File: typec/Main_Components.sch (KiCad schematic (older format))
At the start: 13 parts

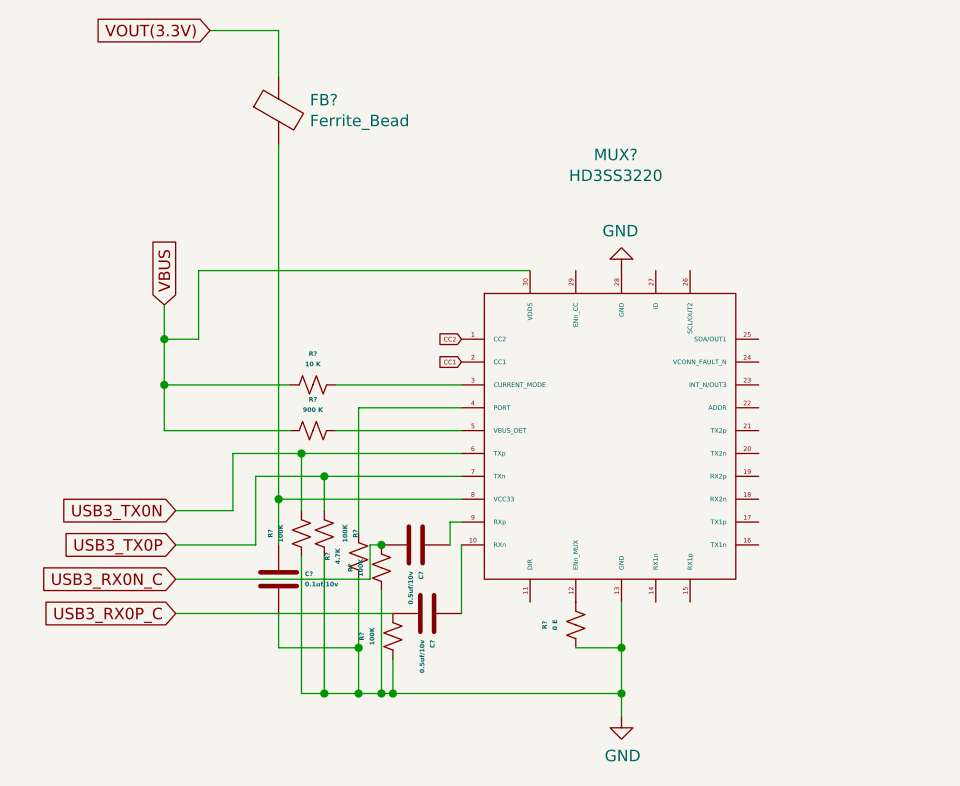
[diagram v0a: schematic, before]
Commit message: Added another page and completed the Multiplexer schematics.
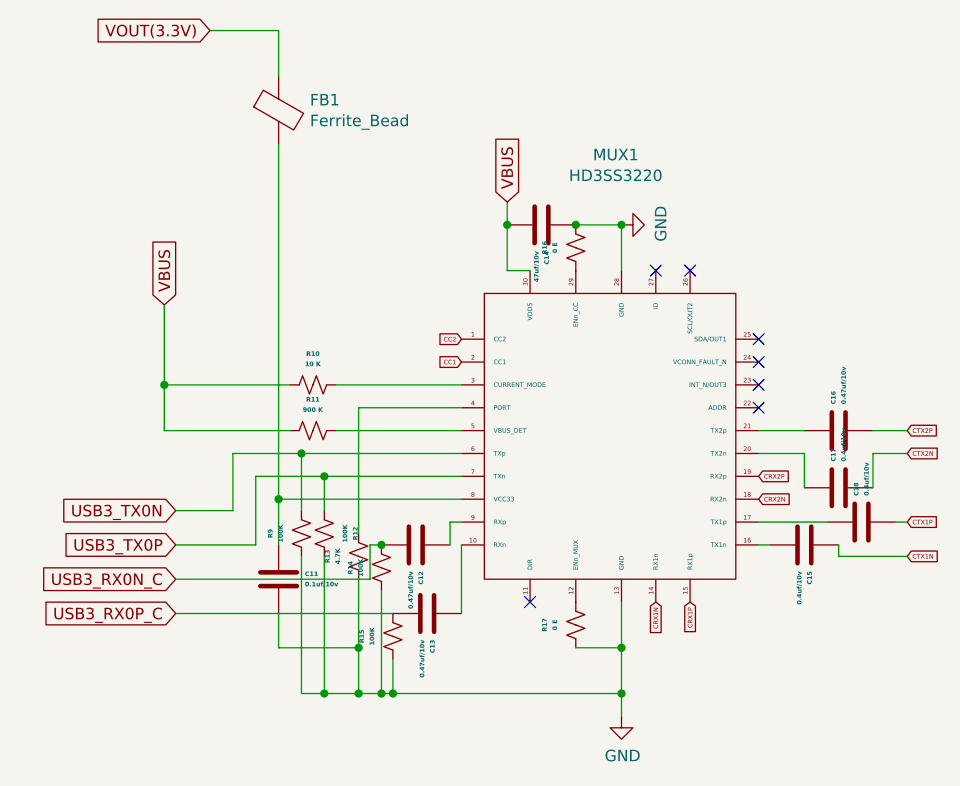
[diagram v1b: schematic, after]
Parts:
- added C14: 47uf/10v, Capacitor_SMD:C_0805_2012Metric, symbol Device:C
- added C15, C17, C18: 0.4uf/10v, Capacitor_SMD:C_0201_0603Metric, symbol Device:C
- added C16: 0.47uf/10v, Capacitor_SMD:C_0201_0603Metric, symbol Device:C
- added R16: 0 E, Resistor_SMD:R_0805_2012Metric, symbol Device:R_Small_US
- C12, C13: renamed from C?; value 0.5uf/10v -> 0.47uf/10v; footprint Capacitor_SMD:C_0805_2012Metric -> Capacitor_SMD:C_0201_0603Metric
- FB1: renamed from FB?; footprint (none) -> Inductor_SMD:L_0805_2012Metric
- MUX1: renamed from MUX?; footprint (none) -> HD3SS3220-VQFN:HD3SS3220-VQFN-MUX
- gave numbers to parts that had none: 9
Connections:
- net GND: now also C14.1, R16.1
- net VBUS: now also C14.2
- net CRX1N: now reaches MUX1.14 (RX1n)
- net CRX1P: now reaches MUX1.15 (RX1p)
- net at MUX1.16 (TX1n): now also C15.2
- net at MUX1.17 (TX1p): now also C18.1
- net CRX2N: now reaches MUX1.18 (RX2n)
- net CRX2P: now reaches MUX1.19 (RX2p)
- net at MUX1.20 (TX2n): now also C17.1
- net at MUX1.21 (TX2p): now also C16.1
- net at MUX1.29 (ENn_CC): now also R16.2
- new net CTX1N: C15.1
- new net CTX1P: C18.2
- new net CTX2N: C17.2
- new net CTX2P: C16.2
- no-connect marks 0 -> 7
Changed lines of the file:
@@
 $EndDescr
 $Comp
-L HD3SS3220-VQFN:HD3SS3220 MUX?
+L HD3SS3220-VQFN:HD3SS3220 MUX1
 U 1 1 5CC0E7BE
 P 4150 4200
-F 0 "MUX?" H 4175 5406 50  0000 C CNN
+F 0 "MUX1" H 4175 5406 50  0000 C CNN
 F 1 "HD3SS3220" H 4175 5315 50  0000 C CNN
-F 2 "" H 4800 3550 50  0001 C CNN
+F 2 "HD3SS3220-VQFN:HD3SS3220-VQFN-MUX" H 4800 3550 50  0001 C CNN
 F 3 "" H 4800 3550 50  0001 C CNN
 	1    4150 4200
@@
 P 4200 5450
 AR Path="/5CC20336" Ref="#PWR?"  Part="1"
-AR Path="/5CC0E3D3/5CC20336" Ref="#PWR?"  Part="1"
-F 0 "#PWR?" H 4200 5200 50  0001 C CNN
+AR Path="/5CC0E3D3/5CC20336" Ref="#PWR0108"  Part="1"
+F 0 "#PWR0108" H 4200 5200 50  0001 C CNN
 F 1 "GND" H 4205 5277 50  0000 C CNN
 F 2 "" H 4200 5450 50  0001 C CNN
@@
 L power:GND #PWR?
 U 1 1 5CC203FA
-P 4200 3500
+P 4200 3300
 AR Path="/5CC203FA" Ref="#PWR?"  Part="1"
-AR Path="/5CC0E3D3/5CC203FA" Ref="#PWR?"  Part="1"
-F 0 "#PWR?" H 4200 3250 50  0001 C CNN
-F 1 "GND" H 4205 3327 50  0000 C CNN
-F 2 "" H 4200 3500 50  0001 C CNN
-F 3 "" H 4200 3500 50  0001 C CNN
-	1    4200 3500
-	-1   0    0    1
+AR Path="/5CC0E3D3/5CC203FA" Ref="#PWR0109"  Part="1"
+F 0 "#PWR0109" H 4200 3050 50  0001 C CNN
+F 1 "GND" H 4205 3127 50  0000 C CNN
+F 2 "" H 4200 3300 50  0001 C CNN
+F 3 "" H 4200 3300 50  0001 C CNN
+	1    4200 3300
+	0    -1   -1   0
 $EndComp
 $Comp
@@
 P 4000 5050
 AR Path="/5CC21E7D" Ref="R?"  Part="1"
-AR Path="/5CC0E3D3/5CC21E7D" Ref="R?"  Part="1"
-F 0 "R?" V 3864 5050 20  0000 C CNB
+AR Path="/5CC0E3D3/5CC21E7D" Ref="R17"  Part="1"
+F 0 "R17" V 3864 5050 20  0000 C CNB
 F 1 "0 E" V 3909 5050 20  0000 C CNB
 F 2 "Resistor_SMD:R_0805_2012Metric" H 4000 5050 50  0001 C CNN
@@
 P 3200 5100
 AR Path="/5CC228F0" Ref="R?"  Part="1"
-AR Path="/5CC0E3D3/5CC228F0" Ref="R?"  Part="1"
-F 0 "R?" V 3064 5100 20  0000 C CNB
+AR Path="/5CC0E3D3/5CC228F0" Ref="R15"  Part="1"
+F 0 "R15" V 3064 5100 20  0000 C CNB
 F 1 "100K" V 3109 5100 20  0000 C CNB
 F 2 "Resistor_SMD:R_0805_2012Metric" H 3200 5100 50  0001 C CNN
@@
 P 3050 4750
 AR Path="/5CC23353" Ref="R?"  Part="1"
-AR Path="/5CC0E3D3/5CC23353" Ref="R?"  Part="1"
-F 0 "R?" V 2914 4750 20  0000 C CNB
+AR Path="/5CC0E3D3/5CC23353" Ref="R13"  Part="1"
+F 0 "R13" V 2914 4750 20  0000 C CNB
 F 1 "4.7K" V 2959 4750 20  0000 C CNB
 F 2 "Resistor_SMD:R_0805_2012Metric" H 3050 4750 50  0001 C CNN
@@
 P 2700 4850
 AR Path="/5CC2436A" Ref="C?"  Part="1"
-AR Path="/5CC0E3D3/5CC2436A" Ref="C?"  Part="1"
-F 0 "C?" H 2815 4873 20  0000 L CNB
+AR Path="/5CC0E3D3/5CC2436A" Ref="C11"  Part="1"
+F 0 "C11" H 2815 4873 20  0000 L CNB
 F 1 "0.1uf/10v" H 2815 4828 20  0000 L CNB
 F 2 "Capacitor_SMD:C_0805_2012Metric" H 2738 4700 20  0001 C CNN
@@
 P 3350 5000
 AR Path="/5CC24594" Ref="C?"  Part="1"
-AR Path="/5CC0E3D3/5CC24594" Ref="C?"  Part="1"
-F 0 "C?" H 3465 5023 20  0000 L CNB
-F 1 "0.5uf/10v" H 3465 4978 20  0000 L CNB
-F 2 "Capacitor_SMD:C_0805_2012Metric" H 3388 4850 20  0001 C CNN
+AR Path="/5CC0E3D3/5CC24594" Ref="C13"  Part="1"
+F 0 "C13" H 3465 5023 20  0000 L CNB
+F 1 "0.47uf/10v" H 3465 4978 20  0000 L CNB
+F 2 "Capacitor_SMD:C_0201_0603Metric" H 3388 4850 20  0001 C CNN
 F 3 "~" H 3350 5000 50  0001 C CNN
 	1    3350 5000
@@
 	2700 4700 2700 4500
 $Comp
-L Device:Ferrite_Bead FB?
+L Device:Ferrite_Bead FB1
 U 1 1 5CC28021
 P 2700 2800
-F 0 "FB?" H 2837 2846 50  0000 L CNN
+F 0 "FB1" H 2837 2846 50  0000 L CNN
 F 1 "Ferrite_Bead" H 2837 2755 50  0000 L CNN
-F 2 "" V 2630 2800 50  0001 C CNN
+F 2 "Inductor_SMD:L_0805_2012Metric" V 2630 2800 50  0001 C CNN
 F 3 "~" H 2700 2800 50  0001 C CNN
 	1    2700 2800
@@
 P 3150 4800
 AR Path="/5CC2DF62" Ref="R?"  Part="1"
-AR Path="/5CC0E3D3/5CC2DF62" Ref="R?"  Part="1"
-F 0 "R?" V 3014 4800 20  0000 C CNB
+AR Path="/5CC0E3D3/5CC2DF62" Ref="R14"  Part="1"
+F 0 "R14" V 3014 4800 20  0000 C CNB
 F 1 "100K" V 3059 4800 20  0000 C CNB
 F 2 "Resistor_SMD:R_0805_2012Metric" H 3150 4800 50  0001 C CNN
@@
 P 3300 4700
 AR Path="/5CC2DF68" Ref="C?"  Part="1"
-AR Path="/5CC0E3D3/5CC2DF68" Ref="C?"  Part="1"
-F 0 "C?" H 3415 4723 20  0000 L CNB
-F 1 "0.5uf/10v" H 3415 4678 20  0000 L CNB
-F 2 "Capacitor_SMD:C_0805_2012Metric" H 3338 4550 20  0001 C CNN
+AR Path="/5CC0E3D3/5CC2DF68" Ref="C12"  Part="1"
+F 0 "C12" H 3415 4723 20  0000 L CNB
+F 1 "0.47uf/10v" H 3415 4678 20  0000 L CNB
+F 2 "Capacitor_SMD:C_0201_0603Metric" H 3338 4550 20  0001 C CNN
 F 3 "~" H 3300 4700 50  0001 C CNN
 	1    3300 4700
@@
 P 2850 4000
 AR Path="/5CC344BF" Ref="R?"  Part="1"
-AR Path="/5CC0E3D3/5CC344BF" Ref="R?"  Part="1"
-F 0 "R?" V 2714 4000 20  0000 C CNB
+AR Path="/5CC0E3D3/5CC344BF" Ref="R10"  Part="1"
+F 0 "R10" V 2714 4000 20  0000 C CNB
 F 1 "10 K" V 2759 4000 20  0000 C CNB
 F 2 "Resistor_SMD:R_0805_2012Metric" H 2850 4000 50  0001 C CNN
@@
 P 2850 4200
 AR Path="/5CC349AC" Ref="R?"  Part="1"
-AR Path="/5CC0E3D3/5CC349AC" Ref="R?"  Part="1"
-F 0 "R?" V 2714 4200 20  0000 C CNB
+AR Path="/5CC0E3D3/5CC349AC" Ref="R11"  Part="1"
+F 0 "R11" V 2714 4200 20  0000 C CNB
 F 1 "900 K" V 2759 4200 20  0000 C CNB
 F 2 "Resistor_SMD:R_0805_2012Metric" H 2850 4200 50  0001 C CNN
@@
 Connection ~ 2200 4000
 Wire Wire Line
-	2200 4000 2200 3800
-Wire Wire Line
 	2950 4000 3500 4000
 Wire Wire Line
@@
 P 2800 4650
 AR Path="/5CC3B665" Ref="R?"  Part="1"
-AR Path="/5CC0E3D3/5CC3B665" Ref="R?"  Part="1"
-F 0 "R?" V 2664 4650 20  0000 C CNB
+AR Path="/5CC0E3D3/5CC3B665" Ref="R9"  Part="1"
+F 0 "R9" V 2664 4650 20  0000 C CNB
 F 1 "100K" V 2709 4650 20  0000 C CNB
 F 2 "Resistor_SMD:R_0805_2012Metric" H 2800 4650 50  0001 C CNN
@@
 P 2900 4650
 AR Path="/5CC3CB7D" Ref="R?"  Part="1"
-AR Path="/5CC0E3D3/5CC3CB7D" Ref="R?"  Part="1"
-F 0 "R?" V 2764 4650 20  0000 C CNB
+AR Path="/5CC0E3D3/5CC3CB7D" Ref="R12"  Part="1"
+F 0 "R12" V 2764 4650 20  0000 C CNB
 F 1 "100K" V 2809 4650 20  0000 C CNB
 F 2 "Resistor_SMD:R_0805_2012Metric" H 2900 4650 50  0001 C CNN
@@
 Text GLabel 3500 3800 0    20   Input ~ 0
 CC2
-Wire Wire Line
-	3800 3500 2350 3500
-Wire Wire Line
-	2350 3500 2350 3800
-Wire Wire Line
-	2350 3800 2200 3800
-Connection ~ 2200 3800
-Wire Wire Line
-	2200 3800 2200 3650
+$Comp
+L Device:C C?
+U 1 1 5CC1BFB9
+P 3850 3300
+AR Path="/5CC1BFB9" Ref="C?"  Part="1"
+AR Path="/5CC0E3D3/5CC1BFB9" Ref="C14"  Part="1"
+F 0 "C14" H 3965 3323 20  0000 L CNB
+F 1 "47uf/10v" H 3965 3278 20  0000 L CNB
+F 2 "Capacitor_SMD:C_0805_2012Metric" H 3888 3150 20  0001 C CNN
+F 3 "~" H 3850 3300 50  0001 C CNN
+	1    3850 3300
+	0    1    1    0
+$EndComp
+$Comp
+L Device:C C?
+U 1 1 5CC1CF3E
+P 5150 4450
+AR Path="/5CC1CF3E" Ref="C?"  Part="1"
+AR Path="/5CC0E3D3/5CC1CF3E" Ref="C17"  Part="1"
+F 0 "C17" H 5265 4473 20  0000 L CNB
+F 1 "0.4uf/10v" H 5265 4428 20  0000 L CNB
+F 2 "Capacitor_SMD:C_0201_0603Metric" H 5188 4300 20  0001 C CNN
+F 3 "~" H 5150 4450 50  0001 C CNN
+	1    5150 4450
+	0    -1   -1   0
+$EndComp
+$Comp
+L Device:C C?
+U 1 1 5CC1EA1F
+P 5150 4200
+AR Path="/5CC1EA1F" Ref="C?"  Part="1"
+AR Path="/5CC0E3D3/5CC1EA1F" Ref="C16"  Part="1"
+F 0 "C16" H 5265 4223 20  0000 L CNB
+F 1 "0.47uf/10v" H 5265 4178 20  0000 L CNB
+F 2 "Capacitor_SMD:C_0201_0603Metric" H 5188 4050 20  0001 C CNN
+F 3 "~" H 5150 4200 50  0001 C CNN
+	1    5150 4200
+	0    -1   -1   0
+$EndComp
+Wire Wire Line
+	2200 3650 2200 4000
+Text GLabel 3700 3200 1    50   Input ~ 0
+VBUS
+$Comp
+L Device:R_Small_US R?
+U 1 1 5CC228A7
+P 4000 3400
+AR Path="/5CC228A7" Ref="R?"  Part="1"
+AR Path="/5CC0E3D3/5CC228A7" Ref="R16"  Part="1"
+F 0 "R16" V 3864 3400 20  0000 C CNB
+F 1 "0 E" V 3909 3400 20  0000 C CNB
+F 2 "Resistor_SMD:R_0805_2012Metric" H 4000 3400 50  0001 C CNN
+F 3 "~" H 4000 3400 50  0001 C CNN
+	1    4000 3400
+	1    0    0    -1
+$EndComp
+Wire Wire Line
+	3800 3500 3700 3500
+Wire Wire Line
+	3700 3500 3700 3300
+Wire Wire Line
+	3700 3200 3700 3300
+Connection ~ 3700 3300
+Wire Wire Line
+	4000 3300 4200 3300
+Connection ~ 4000 3300
+Wire Wire Line
+	4200 3500 4200 3300
+Connection ~ 4200 3300
+Text GLabel 5450 4600 2    20   Input ~ 0
+CTX1P
+Text GLabel 5450 4750 2    20   Input ~ 0
+CTX1N
+Text GLabel 4800 4400 2    20   Input ~ 0
+CRX2P
+Text GLabel 4800 4500 2    20   Input ~ 0
+CRX2N
+Text GLabel 5450 4200 2    20   Input ~ 0
+CTX2P
+Text GLabel 4350 4950 3    20   Input ~ 0
+CRX1N
+Text GLabel 4500 4950 3    20   Input ~ 0
+CRX1P
+Text GLabel 5450 4300 2    20   Input ~ 0
+CTX2N
+Wire Wire Line
+	5300 4200 5450 4200
+Wire Wire Line
+	5000 4200 4800 4200
+Wire Wire Line
+	5300 4300 5450 4300
+Wire Wire Line
+	5000 4300 4800 4300
+Wire Wire Line
+	5000 4300 5000 4450
+Wire Wire Line
+	5300 4450 5300 4300
+$Comp
+L Device:C C?
+U 1 1 5CC4C954
+P 5000 4700
+AR Path="/5CC4C954" Ref="C?"  Part="1"
+AR Path="/5CC0E3D3/5CC4C954" Ref="C15"  Part="1"
+F 0 "C15" H 5115 4723 20  0000 L CNB
+F 1 "0.4uf/10v" H 5115 4678 20  0000 L CNB
+F 2 "Capacitor_SMD:C_0201_0603Metric" H 5038 4550 20  0001 C CNN
+F 3 "~" H 5000 4700 50  0001 C CNN
+	1    5000 4700
+	0    1    1    0
+$EndComp
+$Comp
+L Device:C C?
+U 1 1 5CC4D7CA
+P 5250 4600
+AR Path="/5CC4D7CA" Ref="C?"  Part="1"
+AR Path="/5CC0E3D3/5CC4D7CA" Ref="C18"  Part="1"
+F 0 "C18" H 5365 4623 20  0000 L CNB
+F 1 "0.4uf/10v" H 5365 4578 20  0000 L CNB
+F 2 "Capacitor_SMD:C_0201_0603Metric" H 5288 4450 20  0001 C CNN
+F 3 "~" H 5250 4600 50  0001 C CNN
+	1    5250 4600
+	0    -1   -1   0
+$EndComp
+Wire Wire Line
+	4800 4600 5100 4600
+Wire Wire Line
+	5400 4600 5450 4600
+Wire Wire Line
+	4800 4700 4850 4700
+Wire Wire Line
+	5150 4700 5150 4750
+Wire Wire Line
+	5150 4750 5450 4750
+NoConn ~ 4800 4100
+NoConn ~ 4800 4000
+NoConn ~ 4800 3900
+NoConn ~ 4800 3800
+NoConn ~ 4500 3500
+NoConn ~ 4350 3500
+NoConn ~ 3800 4950
 $EndSCHEMATC
